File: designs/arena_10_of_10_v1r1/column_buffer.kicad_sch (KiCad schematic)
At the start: 24 parts

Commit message: Added initial annotation.
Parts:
- gave numbers to parts that had none: 16

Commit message: Finished footprint assignment.
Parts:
- R100, R101, R102, R103, R104, R105, R98, R99: footprint (none) -> Resistor_SMD:R_0402_1005Metric
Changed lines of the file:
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@@
 			)
 		)
-		(property "Footprint" ""
+		(property "Footprint" "Resistor_SMD:R_0402_1005Metric"
 			(at 93.98 92.71 0)
 			(effects
@@
 			)
 		)
-		(property "Footprint" ""
+		(property "Footprint" "Resistor_SMD:R_0402_1005Metric"
 			(at 93.98 24.13 0)
 			(effects
@@
 			)
 		)
-		(property "Footprint" ""
+		(property "Footprint" "Resistor_SMD:R_0402_1005Metric"
 			(at 57.15 58.42 0)
 			(effects
@@
 			)
 		)
-		(property "Footprint" ""
+		(property "Footprint" "Resistor_SMD:R_0402_1005Metric"
 			(at 93.98 142.24 0)
 			(effects
@@
 			)
 		)
-		(property "Footprint" ""
+		(property "Footprint" "Resistor_SMD:R_0402_1005Metric"
 			(at 93.98 109.22 0)
 			(effects
@@
 			)
 		)
-		(property "Footprint" ""
+		(property "Footprint" "Resistor_SMD:R_0402_1005Metric"
 			(at 93.98 76.2 0)
 			(effects
@@
 			)
 		)
-		(property "Footprint" ""
+		(property "Footprint" "Resistor_SMD:R_0402_1005Metric"
 			(at 93.98 40.64 0)
 			(effects
@@
 			)
 		)
-		(property "Footprint" ""
+		(property "Footprint" "Resistor_SMD:R_0402_1005Metric"
 			(at 93.98 125.73 0)
 			(effects

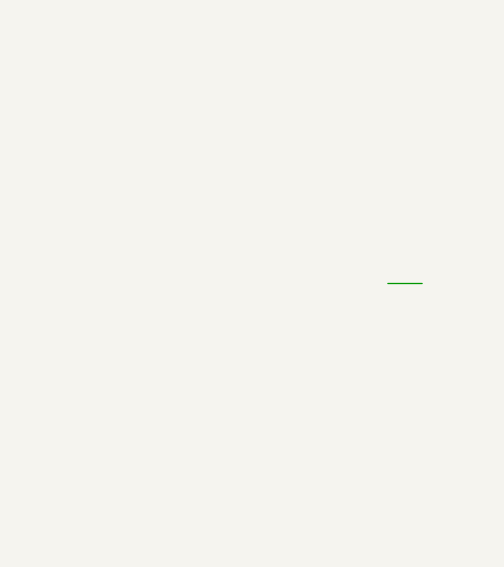
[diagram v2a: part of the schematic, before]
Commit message: Working through schematic design rule check.
Just some power issues remaing.
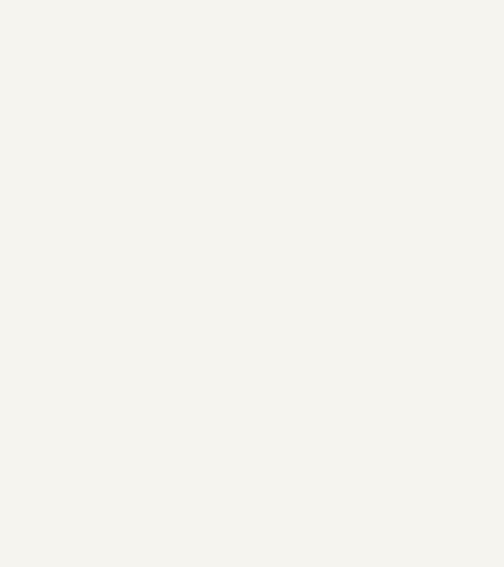
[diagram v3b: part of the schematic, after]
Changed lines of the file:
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@@
-	(wire
-		(pts
-			(xy 236.22 148.59) (xy 232.41 148.59)
-		)
-		(stroke
-			(width 0)
-			(type default)
-		)
-	)
 	(wire
 		(pts

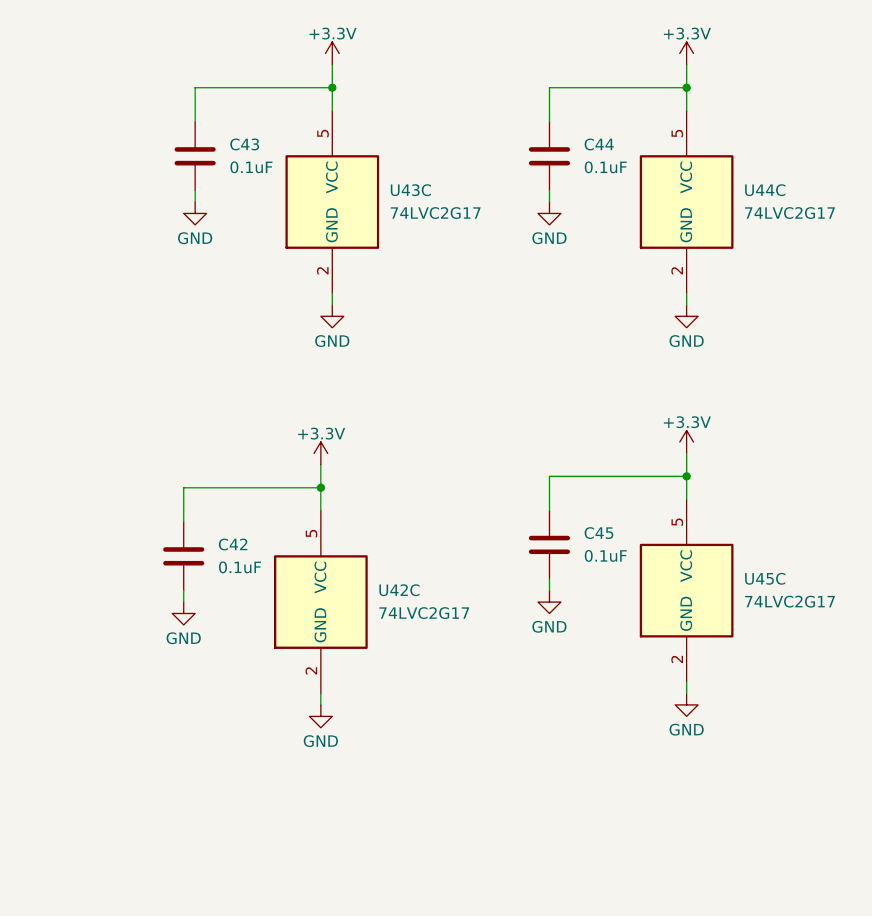
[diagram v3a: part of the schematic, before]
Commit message: Resolved all DSR voilations in schematic.
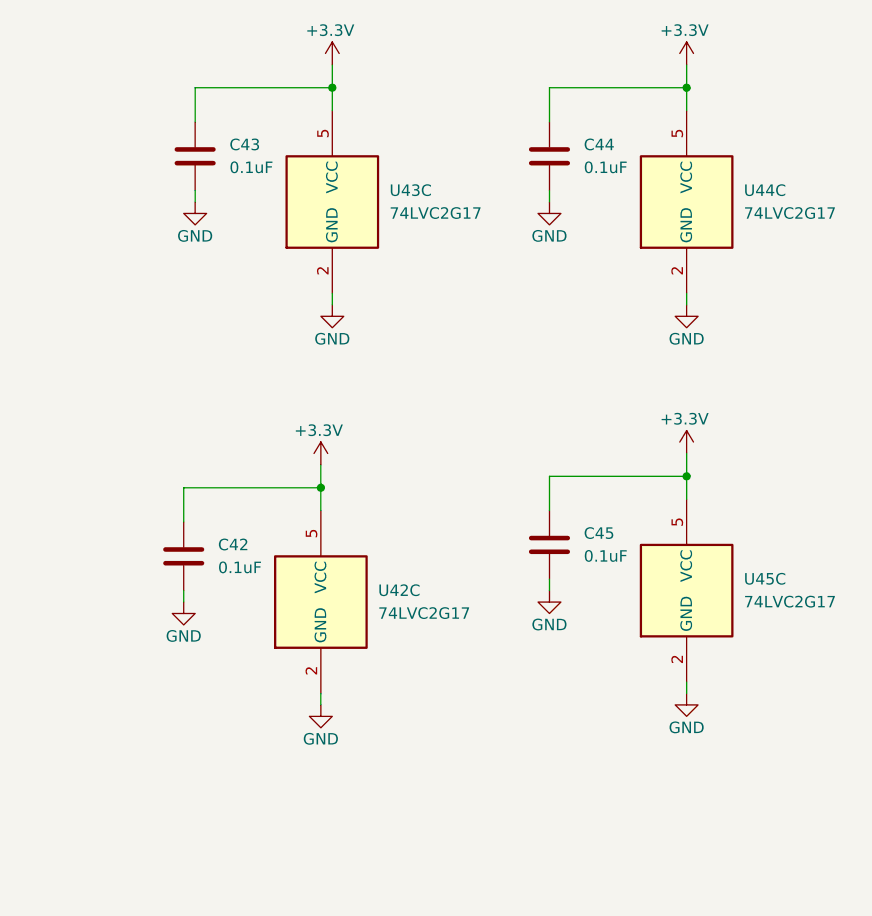
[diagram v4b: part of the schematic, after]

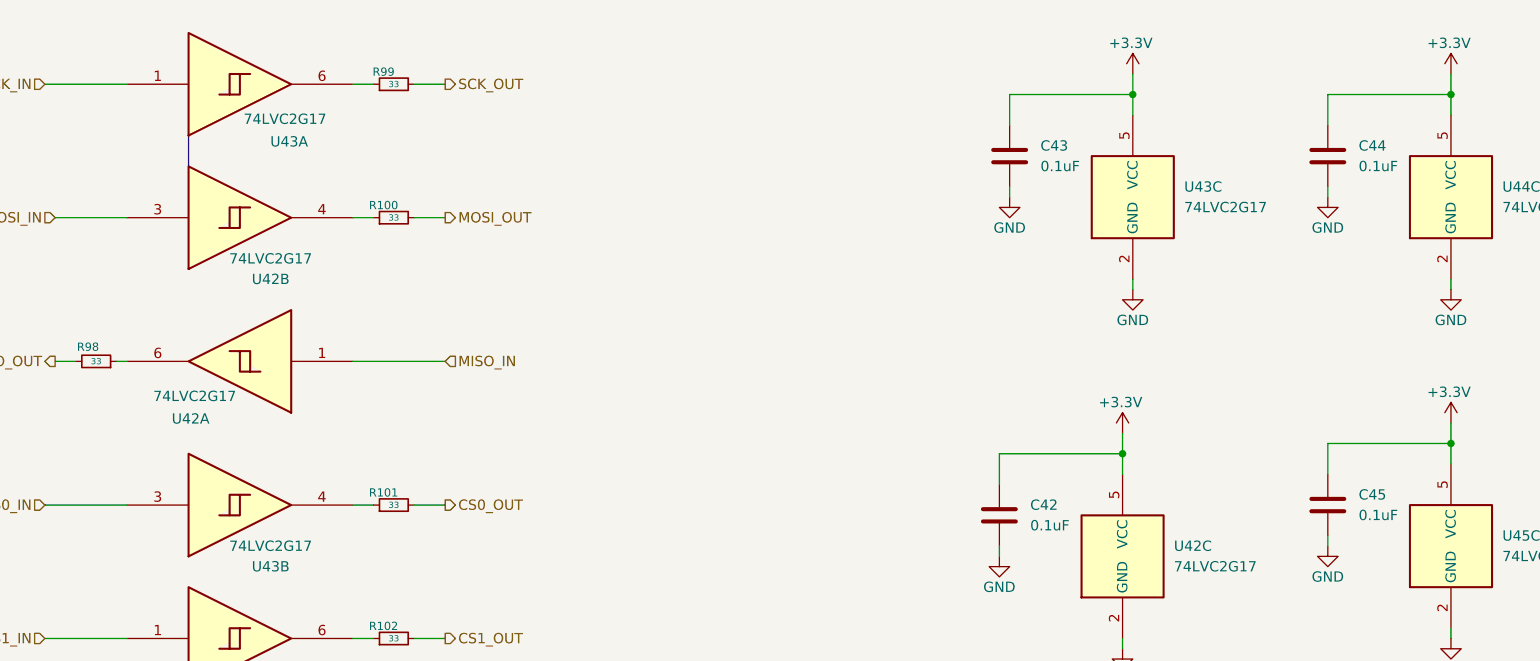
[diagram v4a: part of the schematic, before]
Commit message: Worked on automatic layout of panels + conditioning components.
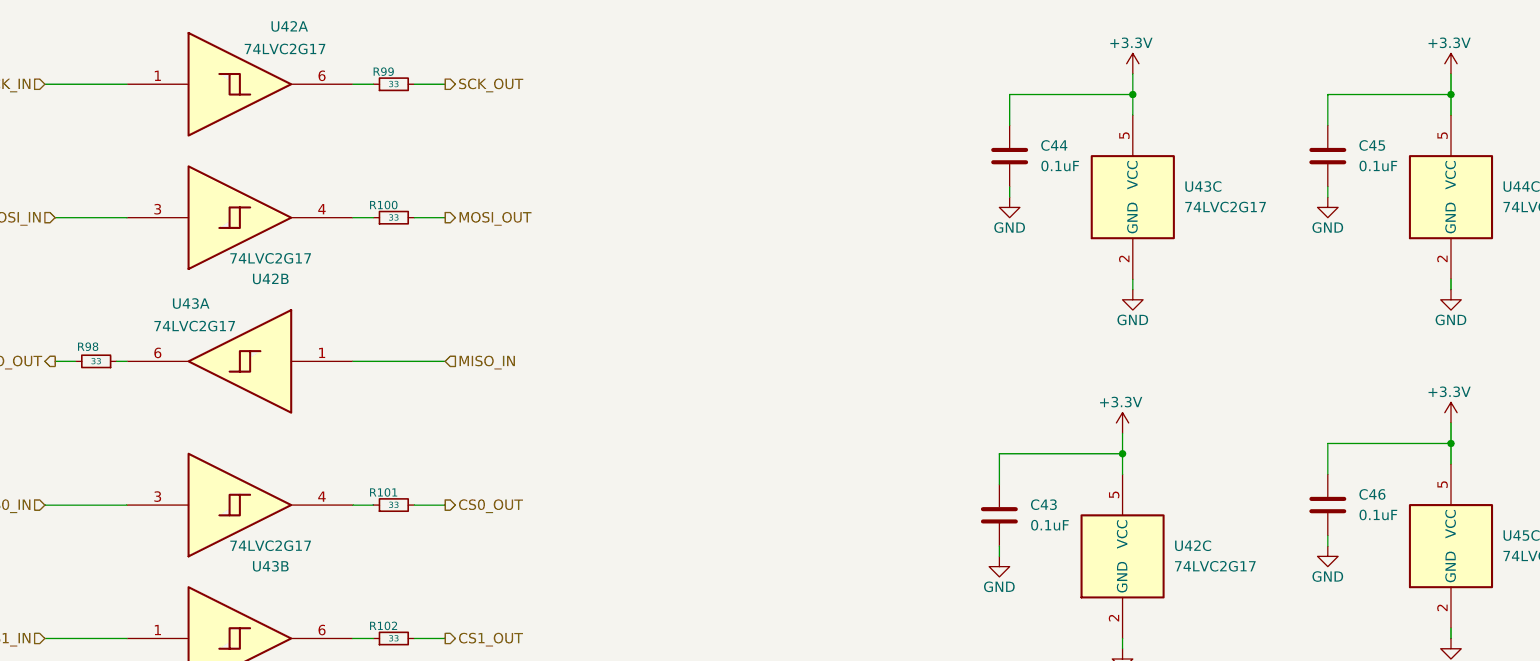
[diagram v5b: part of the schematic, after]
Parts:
- renumbered C42 to C43, C43 to C44, C44 to C45, C45 to C46
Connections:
- net MISO_IN: now also U43.1; no longer U42.1
- net SCK_IN: now also U42.1; no longer U43.1
- net at R99.1: now also U42.6; no longer U43.6
- net at R98.1: now also U43.6; no longer U42.6
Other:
- moved on the sheet: U42A, U43A
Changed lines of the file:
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@@
 		)
 	)
-	(polyline
-		(pts
-			(xy 68.58 30.48) (xy 68.58 34.29)
-		)
-		(stroke
-			(width 0)
-			(type default)
-		)
-	)
 	(wire
 		(pts
@@
 	(symbol
 		(lib_id "74xGxx:74LVC2G17")
-		(at 73.66 58.42 180)
+		(at 76.2 24.13 0)
 		(unit 1)
 		(exclude_from_sim no)
@@
 		(dnp no)
 		(property "Reference" "U42"
-			(at 68.834 65.532 0)
+			(at 81.026 17.018 0)
 			(effects
 				(font
@@
 		)
 		(property "Value" "74LVC2G17"
-			(at 69.342 62.738 0)
+			(at 80.518 19.812 0)
 			(effects
 				(font
@@
 		)
 		(property "Footprint" "Package_TO_SOT_SMD:SOT-23-6"
-			(at 73.66 58.42 0)
+			(at 76.2 24.13 0)
 			(effects
 				(font
@@
 		)
 		(property "Datasheet" "http://www.ti.com/lit/sg/scyt129e/scyt129e.pdf"
-			(at 73.66 58.42 0)
+			(at 76.2 24.13 0)
 			(effects
 				(font
@@
 		)
 		(property "Description" "Dual Buffer, Schmitt Triggered, Low-Voltage CMOS"
-			(at 73.66 58.42 0)
+			(at 76.2 24.13 0)
 			(effects
 				(font
@@
 		(dnp no)
 		(fields_autoplaced yes)
-		(property "Reference" "C44"
+		(property "Reference" "C45"
 			(at 213.36 31.7499 0)
 			(effects
@@
 				)
 				(path "/056666d2-2c8f-491c-bcad-db3c517779a8/3aea6610-f2a3-4b21-99b1-2866223bb12f/3f550e36-6b1c-4366-9cef-eaf43ff57ed4/9cbd2f9c-8fd6-45fc-a308-cb29b4b17e7c"
-					(reference "C44")
+					(reference "C45")
 					(unit 1)
 				)
@@
 		(dnp no)
 		(fields_autoplaced yes)
-		(property "Reference" "C43"
+		(property "Reference" "C44"
 			(at 173.99 31.7499 0)
 			(effects
@@
 				)
 				(path "/056666d2-2c8f-491c-bcad-db3c517779a8/3aea6610-f2a3-4b21-99b1-2866223bb12f/3f550e36-6b1c-4366-9cef-eaf43ff57ed4/9cbd2f9c-8fd6-45fc-a308-cb29b4b17e7c"
-					(reference "C43")
+					(reference "C44")
 					(unit 1)
 				)
@@
 		(dnp no)
 		(fields_autoplaced yes)
-		(property "Reference" "C45"
+		(property "Reference" "C46"
 			(at 213.36 74.9299 0)
 			(effects
@@
 				)
 				(path "/056666d2-2c8f-491c-bcad-db3c517779a8/3aea6610-f2a3-4b21-99b1-2866223bb12f/3f550e36-6b1c-4366-9cef-eaf43ff57ed4/9cbd2f9c-8fd6-45fc-a308-cb29b4b17e7c"
-					(reference "C45")
+					(reference "C46")
 					(unit 1)
 				)
@@
 	(symbol
 		(lib_id "74xGxx:74LVC2G17")
-		(at 76.2 24.13 0)
-		(mirror x)
+		(at 73.66 58.42 0)
+		(mirror y)
 		(unit 1)
 		(exclude_from_sim no)
@@
 		(dnp no)
 		(property "Reference" "U43"
-			(at 81.026 31.242 0)
+			(at 68.834 51.308 0)
 			(effects
 				(font
@@
 		)
 		(property "Value" "74LVC2G17"
-			(at 80.518 28.448 0)
+			(at 69.342 54.102 0)
 			(effects
 				(font
@@
 		)
 		(property "Footprint" "Package_TO_SOT_SMD:SOT-23-6"
-			(at 76.2 24.13 0)
+			(at 73.66 58.42 0)
 			(effects
 				(font
@@
 		)
 		(property "Datasheet" "http://www.ti.com/lit/sg/scyt129e/scyt129e.pdf"
-			(at 76.2 24.13 0)
+			(at 73.66 58.42 0)
 			(effects
 				(font
@@
 		)
 		(property "Description" "Dual Buffer, Schmitt Triggered, Low-Voltage CMOS"
-			(at 76.2 24.13 0)
+			(at 73.66 58.42 0)
 			(effects
 				(font
@@
 		(dnp no)
 		(fields_autoplaced yes)
-		(property "Reference" "C42"
+		(property "Reference" "C43"
 			(at 172.72 76.1999 0)
 			(effects
@@
 				)
 				(path "/056666d2-2c8f-491c-bcad-db3c517779a8/3aea6610-f2a3-4b21-99b1-2866223bb12f/3f550e36-6b1c-4366-9cef-eaf43ff57ed4/9cbd2f9c-8fd6-45fc-a308-cb29b4b17e7c"
-					(reference "C42")
+					(reference "C43")
 					(unit 1)
 				)
